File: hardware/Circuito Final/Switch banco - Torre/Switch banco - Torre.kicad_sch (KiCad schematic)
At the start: 14 parts, among them J1 Conn_01x07_Socket, J2 Conn_01x05_Socket, J3 Conn_02x07_Odd_Even, Q1_1 MMBT2222A, Q3 MMBT2222A, U1 74HC595

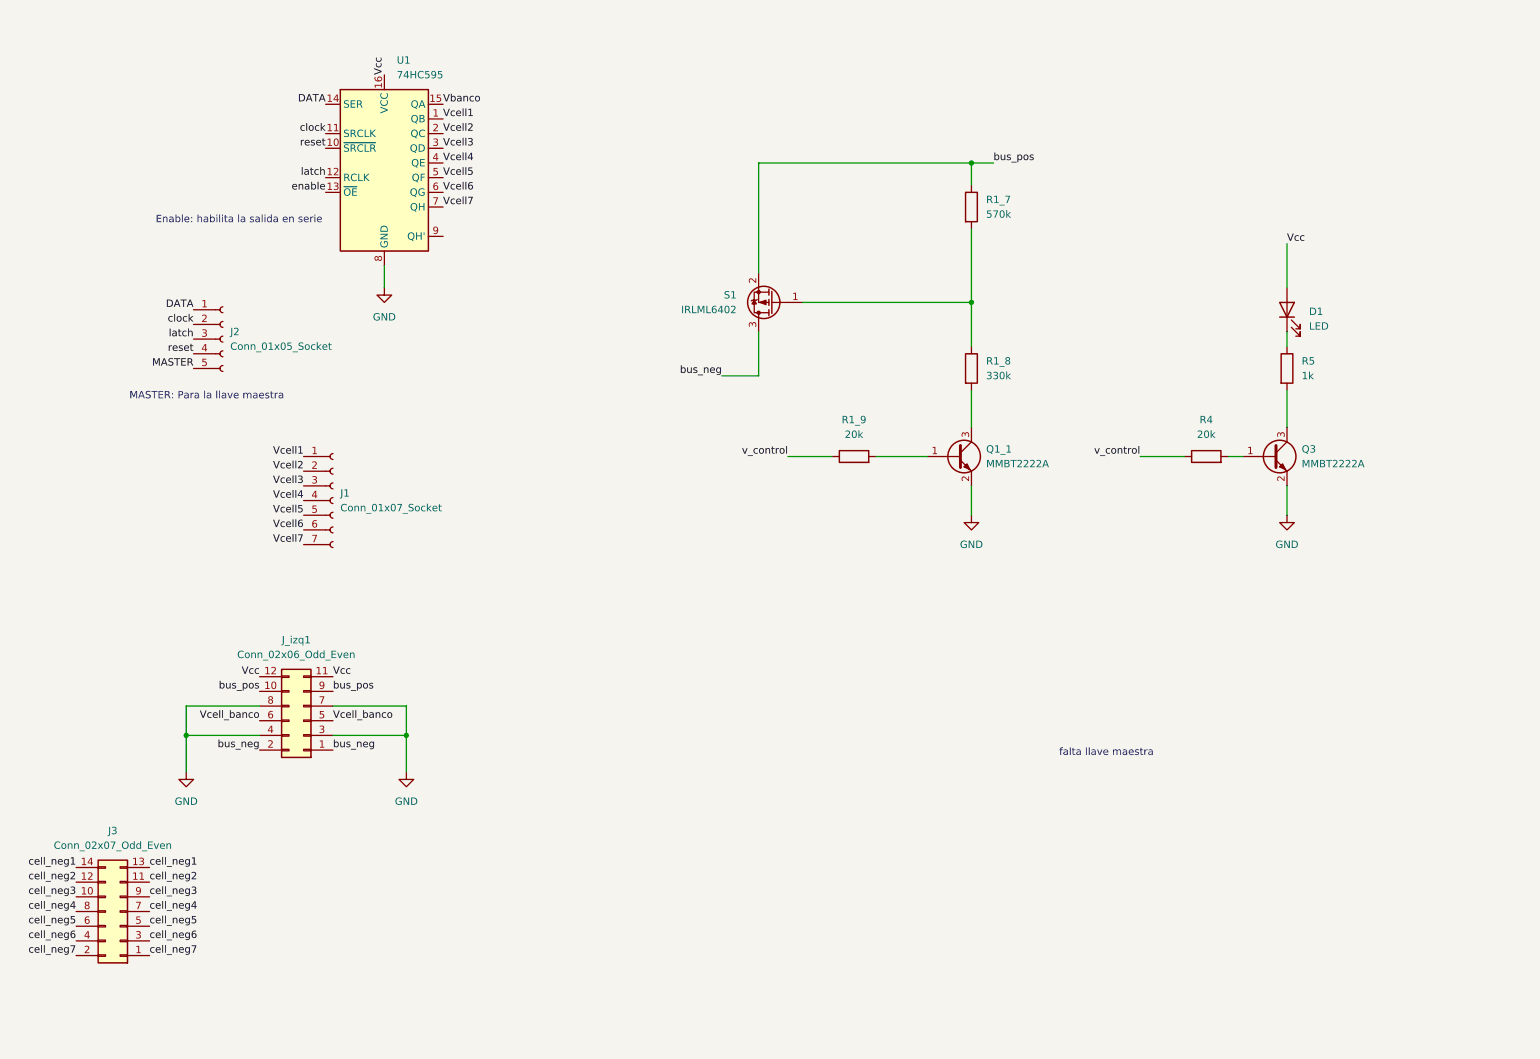
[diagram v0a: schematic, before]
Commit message: sube simu de la salida del shift register con celda
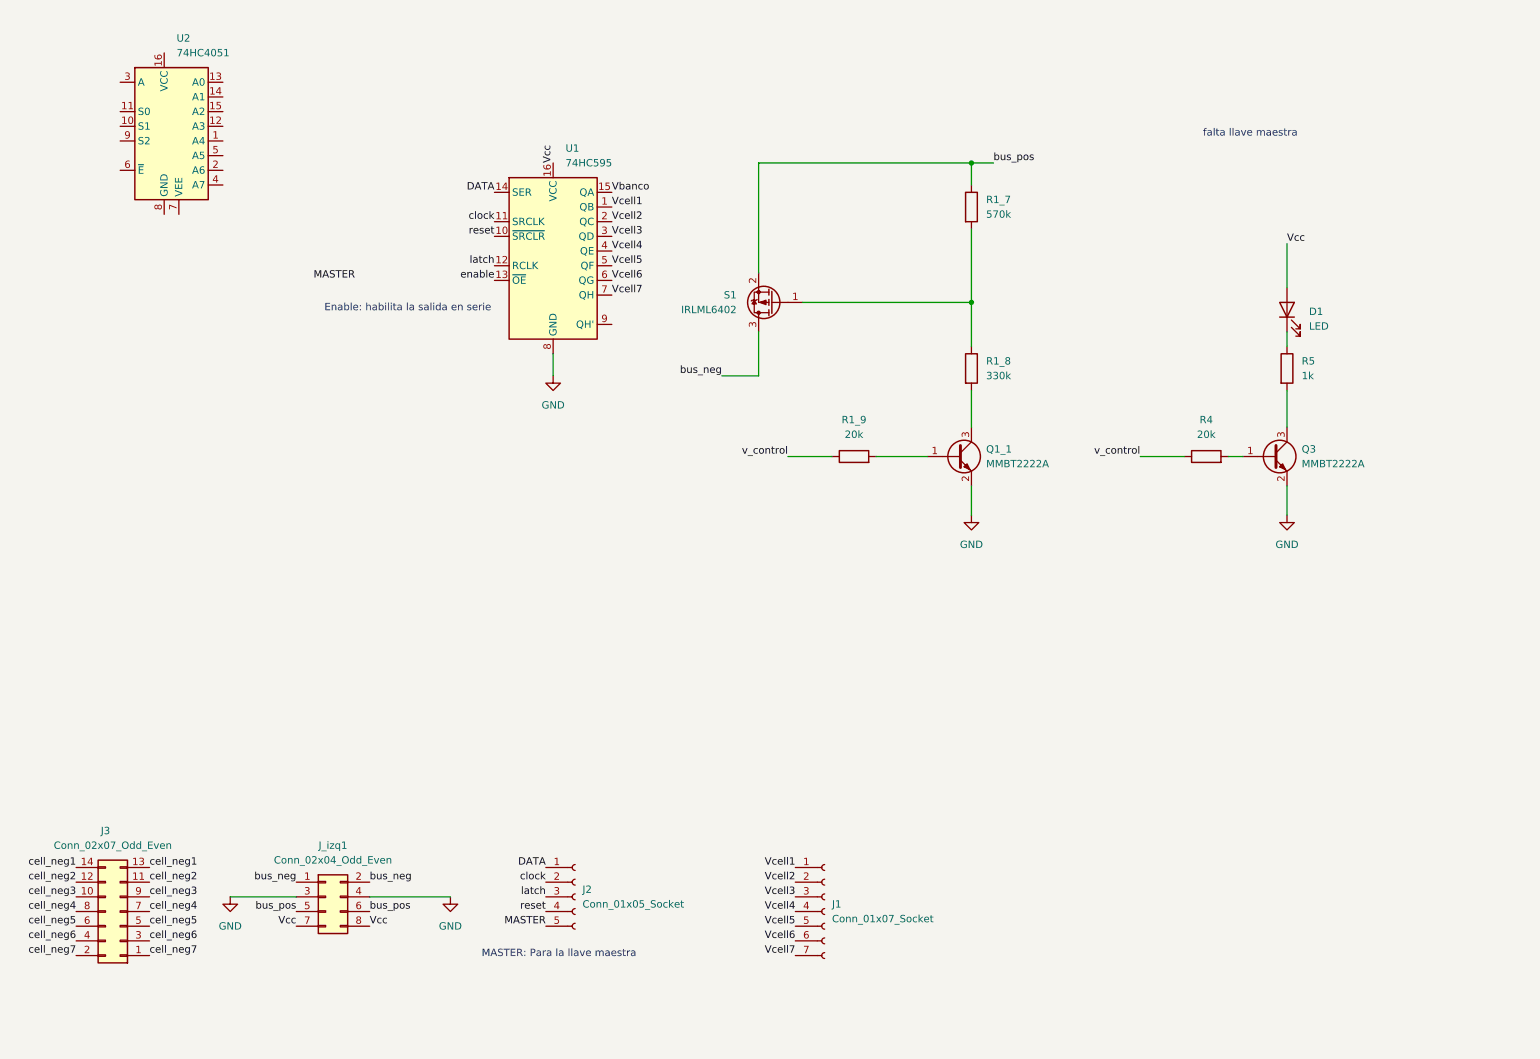
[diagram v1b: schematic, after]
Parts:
- removed J_izq1: Conn_02x06_Odd_Even, Connector_PinSocket_2.54mm:PinSocket_2x06_P2.54mm_Vertical, symbol Connector_Generic:Conn_02x06_Odd_Even
- added J_izq1: Conn_02x04_Odd_Even, Connector_PinSocket_2.54mm:PinSocket_2x04_P2.54mm_Vertical, symbol Connector_Generic:Conn_02x04_Odd_Even
- added U2: 74HC4051, Package_DIP:DIP-16_W7.62mm_SMDSocket_SmallPads, symbol 74xx:74HC4051
- J1: footprint (none) -> Connector_PinSocket_2.54mm:PinSocket_1x07_P2.54mm_Vertical
- J2: footprint (none) -> Connector_PinSocket_2.54mm:PinSocket_1x05_P2.54mm_Vertical
- J3: footprint (none) -> Connector_PinSocket_2.54mm:PinSocket_2x07_P2.54mm_Vertical
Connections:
- net GND: now also J_izq1.3 (Pin_3), J_izq1.4 (Pin_4)
- net Vcc: now also J_izq1.7 (Pin_7), J_izq1.8 (Pin_8)
- net bus_neg: now also J_izq1.1 (Pin_1), J_izq1.2 (Pin_2)
- net bus_pos: now also J_izq1.5 (Pin_5), J_izq1.6 (Pin_6)
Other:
- moved on the sheet: J1, J2, U1

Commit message: sube conexion del shift register en el banco
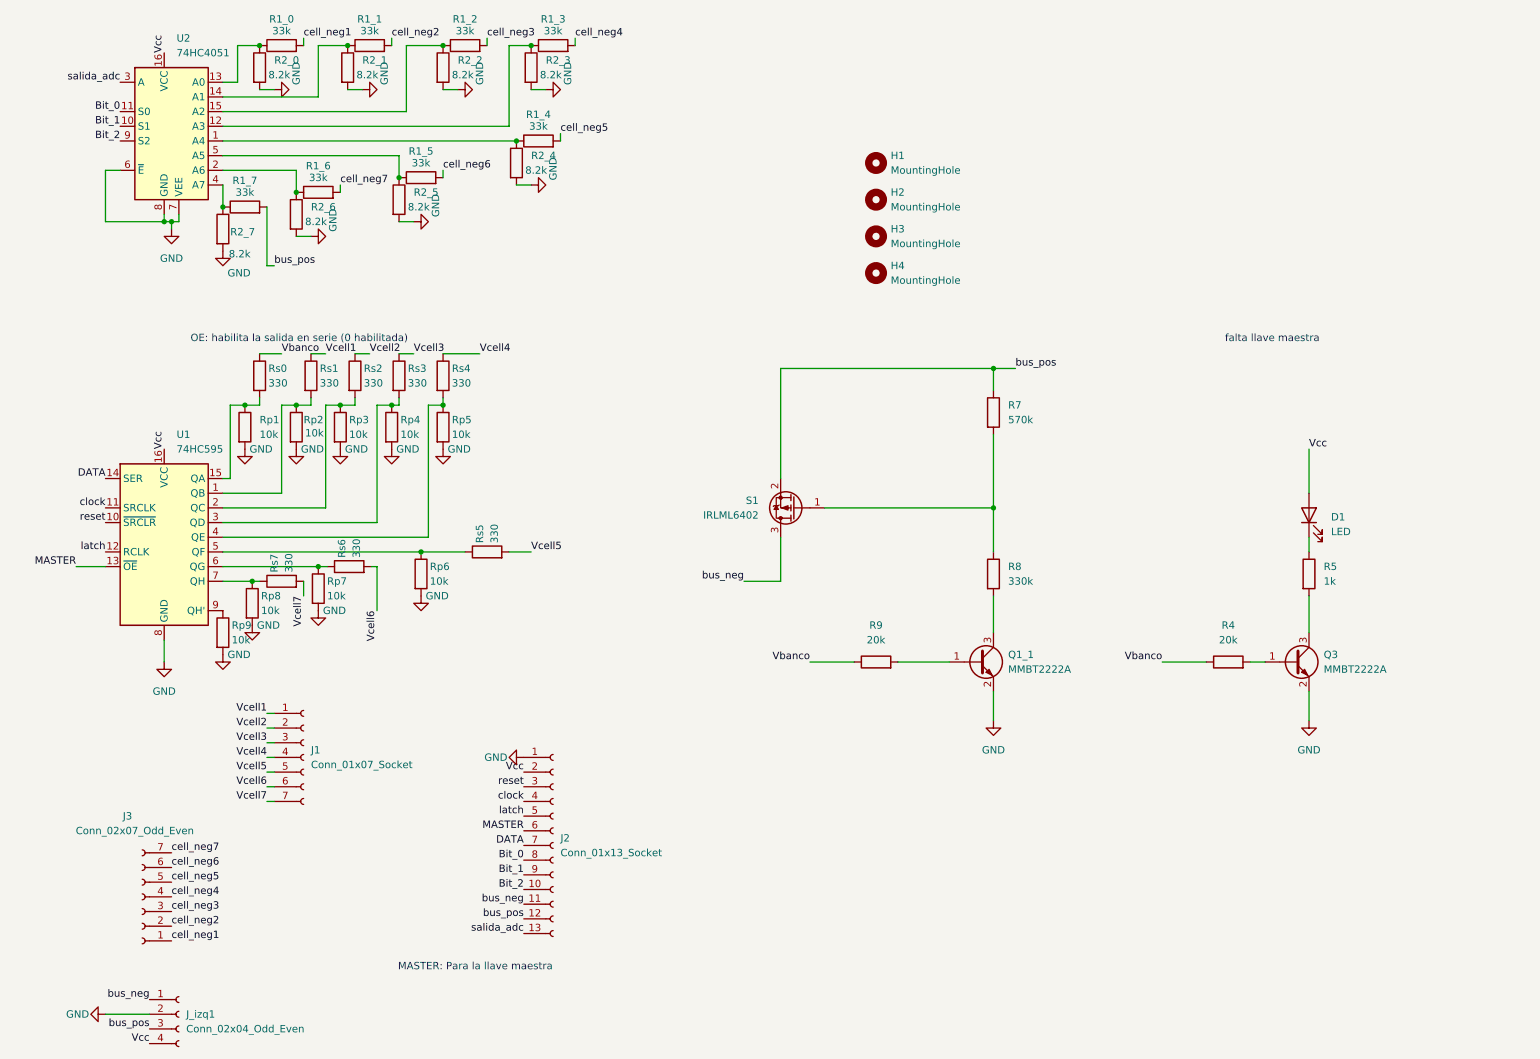
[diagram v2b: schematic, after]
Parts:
- removed J2: Conn_01x05_Socket, Connector_PinSocket_2.54mm:PinSocket_1x05_P2.54mm_Vertical, symbol Connector:Conn_01x05_Socket
- added H1, H2, H3, H4: MountingHole, MountingHole:MountingHole_3.5mm, symbol Mechanical:MountingHole
- added J2: Conn_01x13_Socket, Connector_PinSocket_2.54mm:PinSocket_1x13_P2.54mm_Vertical, symbol Connector:Conn_01x13_Socket
- added R1_0, R1_1, R1_2, R1_3, R1_4, R1_5, R1_6, R1_7: 33k, Resistor_SMD:R_1206_3216Metric_Pad1.30x1.75mm_HandSolder, symbol Device:R
- added R2_0, R2_1, R2_2, R2_3, R2_4, R2_5, R2_6, R2_7: 8.2k, Resistor_SMD:R_1206_3216Metric_Pad1.30x1.75mm_HandSolder, symbol Device:R
- added Rp1, Rp2, Rp3, Rp4, Rp5, Rp6, Rp7, Rp8, Rp9: 10k, Resistor_SMD:R_1206_3216Metric_Pad1.30x1.75mm_HandSolder, symbol Device:R
- added Rs0, Rs1, Rs2, Rs3, Rs4, Rs5, Rs6, Rs7: 330, Resistor_SMD:R_1206_3216Metric_Pad1.30x1.75mm_HandSolder, symbol Device:R
- D1: footprint LED_THT:LED_D1.8mm_W1.8mm_H2.4mm_Horizontal_O1.27mm_Z1.6mm -> LED_THT:LED_D5.0mm
- J3: footprint Connector_PinSocket_2.54mm:PinSocket_2x07_P2.54mm_Vertical -> Connector_PinSocket_2.54mm:PinSocket_1x07_P2.54mm_Vertical; symbol Connector_Generic:Conn_02x07_Odd_Even -> Connector:Conn_01x07_Socket
- J_izq1: footprint Connector_PinSocket_2.54mm:PinSocket_2x04_P2.54mm_Vertical -> Connector_PinSocket_2.54mm:PinSocket_1x04_P2.54mm_Vertical; symbol Connector_Generic:Conn_02x04_Odd_Even -> Connector:Conn_01x04_Socket
- renumbered R1_7 to R7, R1_8 to R8, R1_9 to R9
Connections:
- net enable is gone; now on net MASTER: U1.13 (~{OE})
- net v_control is gone; now on net Vbanco: R4.1, R9.1
- net DATA: now also J2.7 (Pin_7)
- net GND: now also J_izq1.2 (Pin_2), U2.6 (~{E}), U2.7 (VEE), U2.8 (GND), J2.1 (Pin_1), R2_0.2, R2_1.2, R2_2.2, R2_3.2, R2_4.2, R2_5.2, R2_6.2, R2_7.2, Rp1.2, Rp2.2, Rp3.2, Rp4.2, Rp5.2, Rp6.2, Rp7.2, Rp8.2, Rp9.2; no longer J_izq1.3 (Pin_3), J_izq1.4 (Pin_4)
- net MASTER: now also J2.6 (Pin_6)
- net Vbanco: now also Rs0.1; no longer U1.15 (QA)
- net Vcc: now also J_izq1.4 (Pin_4), U2.16 (VCC), J2.2 (Pin_2); no longer J_izq1.7 (Pin_7), J_izq1.8 (Pin_8)
- net Vcell1: now also Rs1.1; no longer U1.1 (QB)
- net Vcell2: now also Rs2.1; no longer U1.2 (QC)
- net Vcell3: now also Rs3.1; no longer U1.3 (QD)
- net Vcell4: now also Rs4.1; no longer U1.4 (QE)
- net Vcell5: now also Rs5.2; no longer U1.5 (QF)
- net Vcell6: now also Rs6.2; no longer U1.6 (QG)
- net Vcell7: now also Rs7.2; no longer U1.7 (QH)
- net bus_neg: now also J2.11 (Pin_11); no longer J_izq1.2 (Pin_2)
- net bus_pos: now also J_izq1.3 (Pin_3), J2.12 (Pin_12), R1_7.2; no longer J_izq1.5 (Pin_5), J_izq1.6 (Pin_6)
- net cell_neg1: now also J3.1 (Pin_1), R1_0.2; no longer J3.13 (Pin_13), J3.14 (Pin_14)
- net cell_neg2: now also J3.2 (Pin_2), R1_1.2; no longer J3.11 (Pin_11), J3.12 (Pin_12)
- net cell_neg3: now also J3.3 (Pin_3), R1_2.2; no longer J3.10 (Pin_10), J3.9 (Pin_9)
- net cell_neg4: now also J3.4 (Pin_4), R1_3.2; no longer J3.7 (Pin_7), J3.8 (Pin_8)
- net cell_neg5: now also R1_4.2; no longer J3.6 (Pin_6)
- net cell_neg6: now also J3.6 (Pin_6), R1_5.2; no longer J3.3 (Pin_3), J3.4 (Pin_4)
- net cell_neg7: now also J3.7 (Pin_7), R1_6.2; no longer J3.1 (Pin_1), J3.2 (Pin_2)
- net clock: now also J2.4 (Pin_4)
- net latch: now also J2.5 (Pin_5)
- net reset: now also J2.3 (Pin_3)
- net at U2.1 (A4): now also R1_4.1, R2_4.1
- net Bit_1: now reaches U2.10 (S1)
- net Bit_1: now also J2.9 (Pin_9)
- net Bit_0: now reaches U2.11 (S0)
- net Bit_0: now also J2.8 (Pin_8)
- net at U2.12 (A3): now also R1_3.1, R2_3.1
- net at U2.13 (A0): now also R1_0.1, R2_0.1
- net at U2.14 (A1): now also R1_1.1, R2_1.1
- net at U2.15 (A2): now also R1_2.1, R2_2.1
- net at U2.2 (A6): now also R1_6.1, R2_6.1
- net salida_adc: now reaches U2.3 (A)
- net salida_adc: now also J2.13 (Pin_13)
- net at U2.4 (A7): now also R1_7.1, R2_7.1
- net at U2.5 (A5): now also R1_5.1, R2_5.1
- net Bit_2: now reaches U2.9 (S2)
- net Bit_2: now also J2.10 (Pin_10)
- net at U1.9 (QH'): now also Rp9.1
- new net: Rp1.1, Rs0.2, U1.15 (QA)
- new net: Rp7.1, Rs6.1, U1.6 (QG)
- new net: Rp4.1, Rs3.2, U1.3 (QD)
- new net: Rp3.1, Rs2.2, U1.2 (QC)
- new net: Rp6.1, Rs5.1, U1.5 (QF)
- new net: Rp2.1, Rs1.2, U1.1 (QB)
- new net: Rp5.1, Rs4.2, U1.4 (QE)
- new net: Rp8.1, Rs7.1, U1.7 (QH)
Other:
- note added: "OE: habilita la salida en serie (0 habilitada)"
- note removed: "Enable: habilita la salida en serie"
- moved on the sheet: D1, J1, Q1_1, Q3, R4, R5, R7, R8, R9, S1, U1

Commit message: conecta los integrados en el pcb del banco
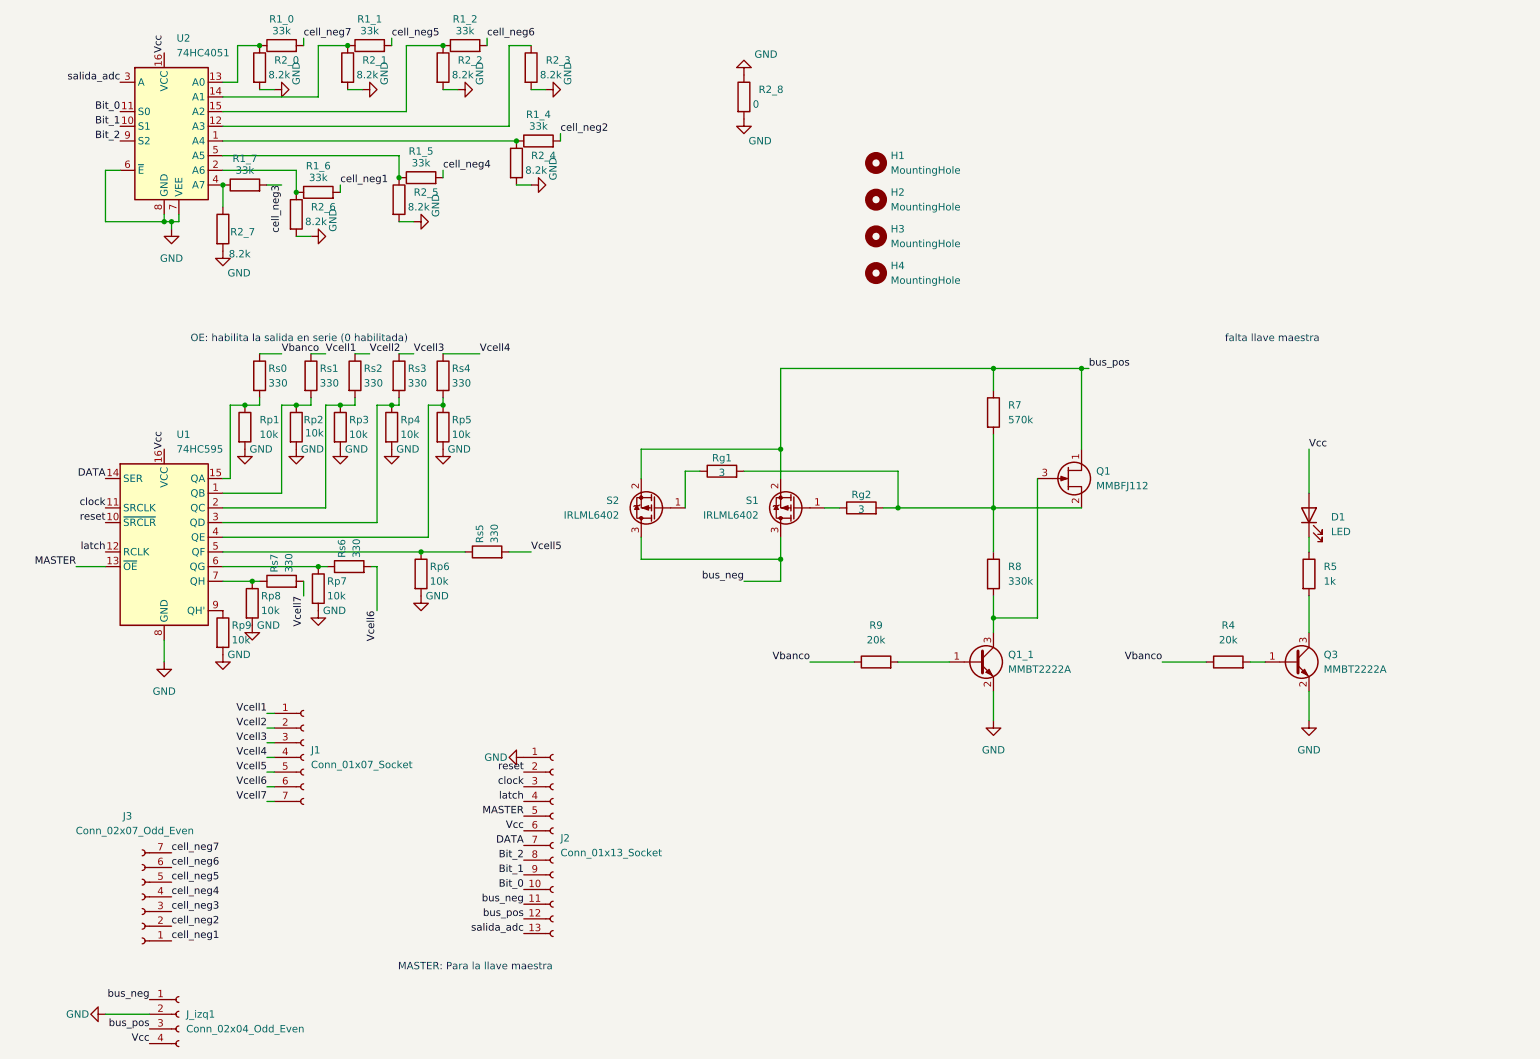
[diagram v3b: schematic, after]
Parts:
- removed R1_3: 33k, Resistor_SMD:R_1206_3216Metric_Pad1.30x1.75mm_HandSolder, symbol Device:R
- added Q1: MMBFJ112, Package_TO_SOT_SMD:SOT-23_Handsoldering, symbol Transistor_FET:MMBFJ112
- added R2_8: 0, Resistor_SMD:R_1206_3216Metric_Pad1.30x1.75mm_HandSolder, symbol Device:R
- added Rg1, Rg2: 3, Resistor_SMD:R_1206_3216Metric_Pad1.30x1.75mm_HandSolder, symbol Device:R
- added S2: IRLML6402, Package_TO_SOT_SMD:SOT-23_Handsoldering, symbol Transistor_FET:IRLML6402
- H1, H2, H3, H4: footprint MountingHole:MountingHole_3.5mm -> modificados:MountingHole_3.5mm
- Q1_1, Q3, S1: footprint Package_TO_SOT_SMD:SOT-23 -> Package_TO_SOT_SMD:SOT-23_Handsoldering
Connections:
- net Bit_0: now also J2.10 (Pin_10); no longer J2.8 (Pin_8)
- net Bit_2: now also J2.8 (Pin_8); no longer J2.10 (Pin_10)
- net GND: now also R2_8.1, R2_8.2
- net MASTER: now also J2.5 (Pin_5); no longer J2.6 (Pin_6)
- net Vcc: now also J2.6 (Pin_6); no longer J2.2 (Pin_2)
- net bus_neg: now also S2.3 (D)
- net bus_pos: now also Q1.1 (D), S2.2 (S); no longer R1_7.2
- net cell_neg1: now also R1_6.2; no longer R1_0.2
- net cell_neg2: now also R1_4.2; no longer R1_1.2
- net cell_neg3: now also R1_7.2; no longer R1_2.2
- net cell_neg4: now also R1_5.2
- net cell_neg5: now also R1_1.2; no longer R1_4.2
- net cell_neg6: now also R1_2.2; no longer R1_5.2
- net cell_neg7: now also R1_0.2; no longer R1_6.2
- net clock: now also J2.3 (Pin_3); no longer J2.4 (Pin_4)
- net latch: now also J2.4 (Pin_4); no longer J2.5 (Pin_5)
- net reset: now also J2.2 (Pin_2); no longer J2.3 (Pin_3)
- net at R7.2, R8.1: now also Q1.2 (S), Rg1.2, Rg2.2; no longer S1.1 (G)
- net at Q1_1.3 (C), R8.2: now also Q1.3 (G)
- new net: Rg1.1, S2.1 (G)
- new net: Rg2.1, S1.1 (G)

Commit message: sube pcb del banco todo conectado
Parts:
- removed J2: Conn_01x13_Socket, Connector_PinSocket_2.54mm:PinSocket_1x13_P2.54mm_Vertical, symbol Connector:Conn_01x13_Socket
- added F1: Fuse, Fuse:Fuse_1206_3216Metric_Pad1.42x1.75mm_HandSolder, symbol Device:Fuse
- added J2: Conn_02x07_Odd_Even, Connector_IDC:IDC-Header_2x07_P2.54mm_Horizontal, symbol Connector_Generic:Conn_02x07_Odd_Even
- added R2_10, R2_9: 0, Resistor_SMD:R_1206_3216Metric_Pad1.30x1.75mm_HandSolder, symbol Device:R
- added TP1: TestPoint, TestPoint:TestPoint_Loop_D2.54mm_Drill1.5mm_Beaded, symbol Connector:TestPoint
- J1: value Conn_01x07_Socket -> Conn_01x07
- J3: value Conn_02x07_Odd_Even -> Conn_01x07
- J_izq1: value Conn_02x04_Odd_Even -> Conn_01x04
- Rg1, Rg2: value 3 -> 100
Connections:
- net MASTER is gone; now on net GND: U1.13 (~{OE})
- net Bit_0: now also J2.2 (Pin_2)
- net Bit_1: now also J2.1 (Pin_1)
- net Bit_2: now also J2.3 (Pin_3)
- net DATA: now also J2.11 (Pin_11)
- net GND: now also J2.10 (Pin_10), R2_10.1, R2_10.2, R2_9.1, R2_9.2
- net Vcc: now also J2.9 (Pin_9)
- net bus_neg: now also F1.2, J2.7 (Pin_7), J2.8 (Pin_8); no longer S1.3 (D), S2.3 (D)
- net bus_pos: now also J2.5 (Pin_5), J2.6 (Pin_6)
- net clock: now also J2.14 (Pin_14)
- net latch: now also J2.13 (Pin_13)
- net reset: now also J2.12 (Pin_12)
- net salida_adc: now also J2.4 (Pin_4)
- net at Q1.2 (S), R7.2, R8.1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: now also TP1.1
- new net: F1.1, S1.3 (D), S2.3 (D)
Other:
- note removed: "MASTER: Para la llave maestra"
- moved on the sheet: D1, H1, H2, H3, H4, J1, Q1, Q1_1, Q3, R2_8, R4, R5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
